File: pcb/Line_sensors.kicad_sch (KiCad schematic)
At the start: 31 parts, among them Q2 BC817, U10 CNY70, U4 CNY70, U5 CNY70, U6 CNY70, U7 CNY70, U8 CNY70, U9 CNY70

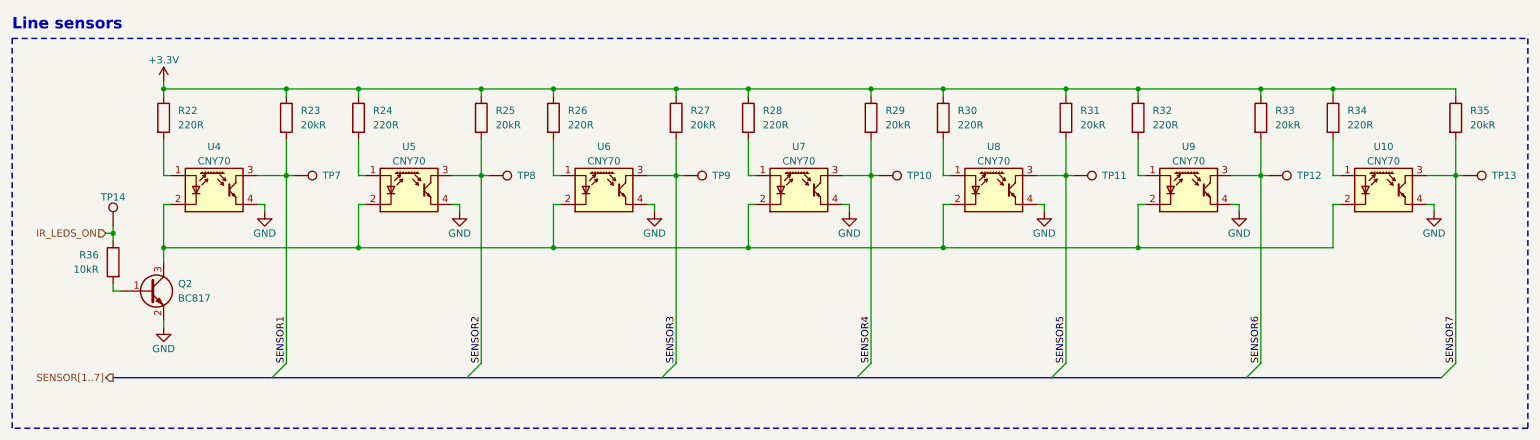
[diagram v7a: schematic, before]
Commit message: [pcb] 4 layer PCB
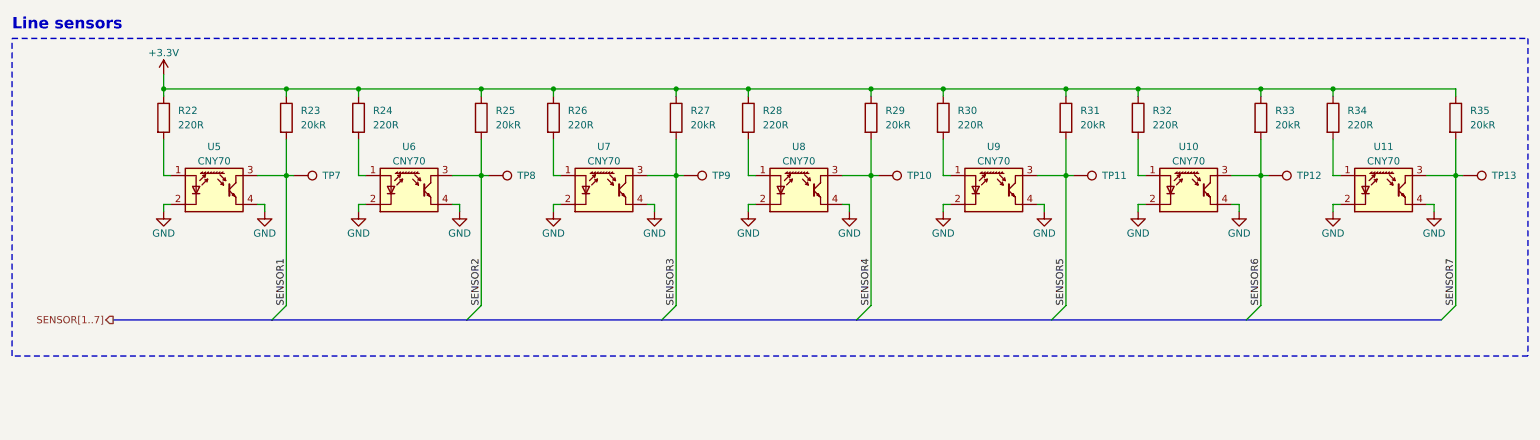
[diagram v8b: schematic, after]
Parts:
- removed Q2: BC817, Package_TO_SOT_SMD:SOT-23, symbol Transistor_BJT:BC817
- removed R36: 10kR, Resistor_SMD:R_0805_2012Metric, symbol Device:R
- removed TP14: TestPoint, TestPoint:TestPoint_Pad_D2.0mm, symbol Connector:TestPoint
- renumbered U9 to U10, U10 to U11, U4 to U5, U5 to U6, U6 to U7, U7 to U8, U8 to U9
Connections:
- net GND: now also U10.2 (K), U11.2 (K), U5.2 (K), U6.2 (K), U7.2 (K), U8.2 (K), U9.2 (K)
